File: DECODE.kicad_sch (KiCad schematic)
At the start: 16 parts

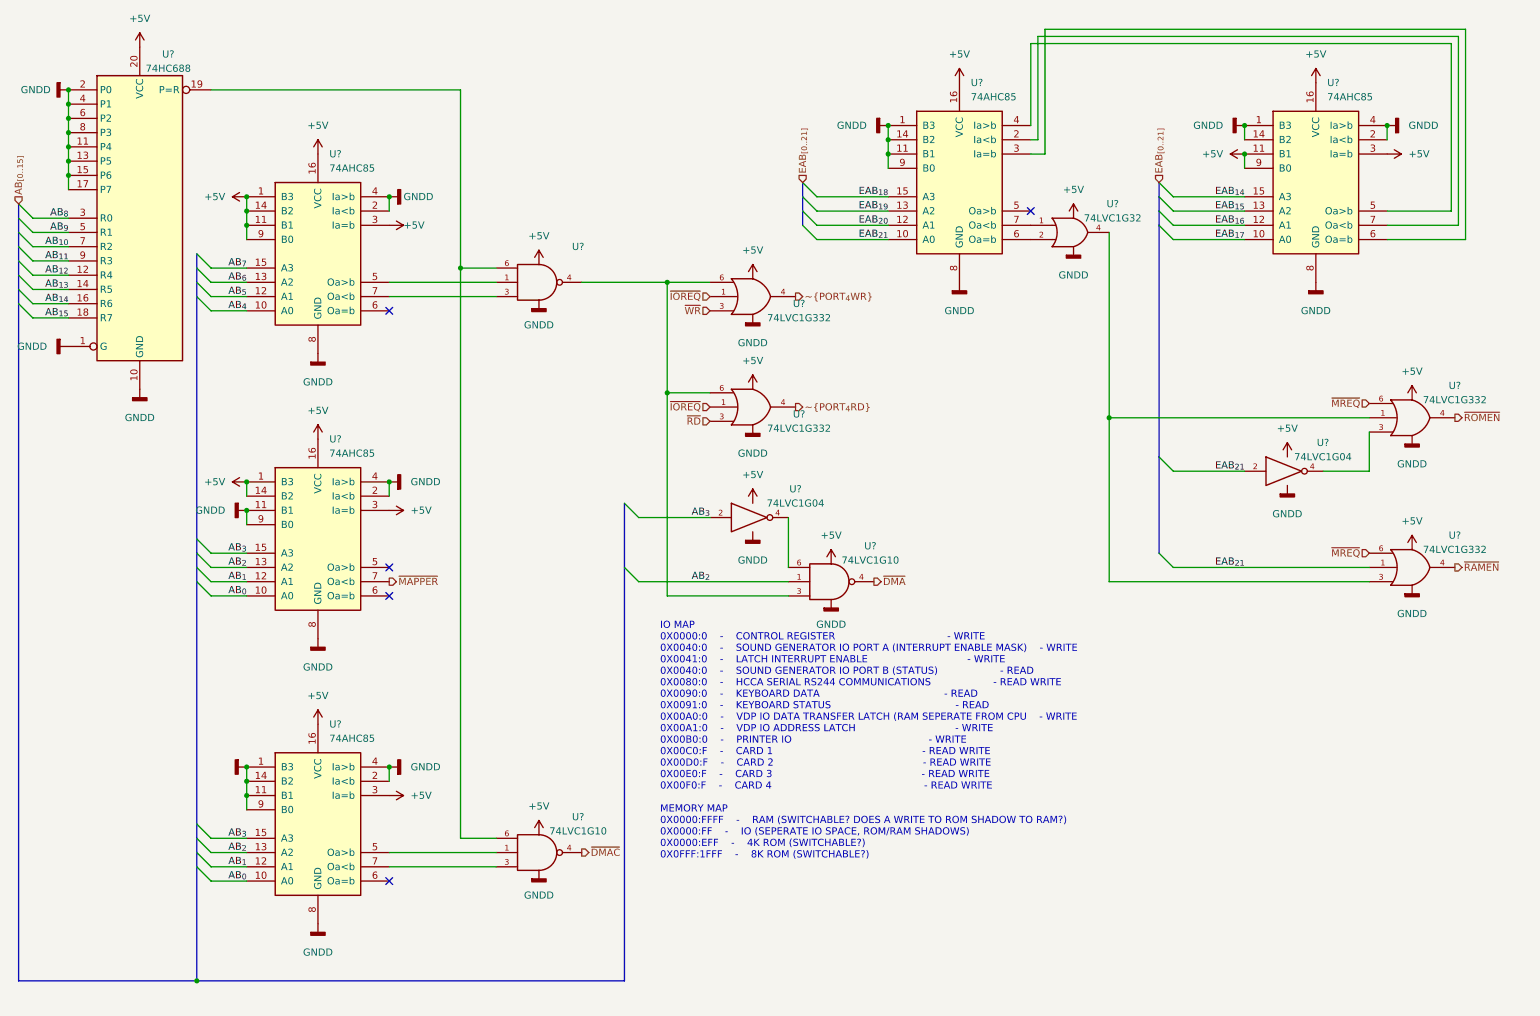
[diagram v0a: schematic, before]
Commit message: added decoupling capacitors, perhaps too many? idk better more than less!
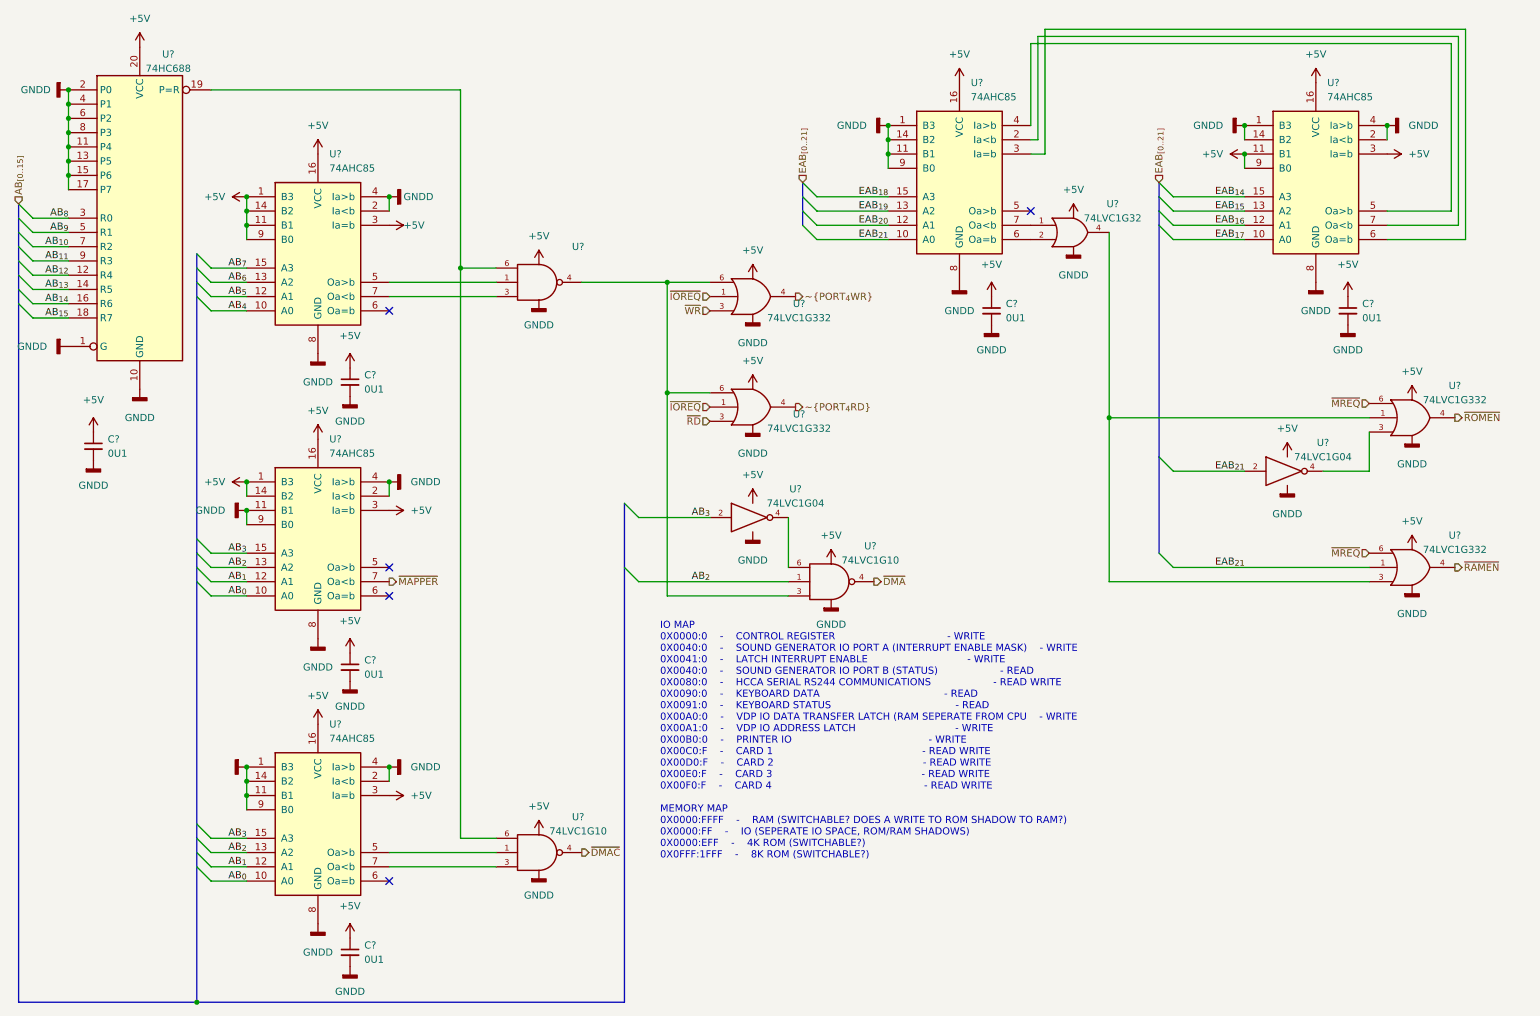
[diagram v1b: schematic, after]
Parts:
- added C? (x6): 0U1, symbol Device:C_Small
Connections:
- net +5V: now also C?.1, C?.1, C?.1, C?.1, C?.1, C?.1
- net GND: now also C?.2, C?.2, C?.2, C?.2, C?.2, C?.2

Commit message: some clean up and simplification, as well as some renaming
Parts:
- removed U?: ~, symbol 74xGxx:74LVC1G10
- added U63: (no value), symbol 74xGxx:74LVC1G10
- gave numbers to parts that had none: 21
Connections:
- net +5V: now also U63.5 (VCC)
- net GND: now also U63.2 (GND)
- net at U60.5 (Oa>b): now also U63.1
- net at U60.7 (Oa<b): now also U63.3
- net at U65.6, U66.6, U68.3: now also U63.4
- net at U59.19 (P=R), U64.6: now also U63.6
- net AB_{0} renamed AB0
- net AB_{10} renamed AB10
- net AB_{11} renamed AB11
- net AB_{12} renamed AB12
- net AB_{13} renamed AB13
- net AB_{14} renamed AB14
- net AB_{15} renamed AB15
- net AB_{1} renamed AB1
- net AB_{2} renamed AB2
- net AB_{3} renamed AB3
- net AB_{4} renamed AB4
- net AB_{5} renamed AB5
- net AB_{6} renamed AB6
- net AB_{7} renamed AB7
- net AB_{8} renamed AB8
- net AB_{9} renamed AB9
- net EAB_{14} renamed EAB14
- net EAB_{15} renamed EAB15
- net EAB_{16} renamed EAB16
- net EAB_{17} renamed EAB17
- net EAB_{18} renamed EAB18
- net EAB_{19} renamed EAB19
- net EAB_{20} renamed EAB20
- net EAB_{21} renamed EAB21

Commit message: begin integration of logic into atf1508
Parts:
- C33, C34, C35, C36, C37, C38: footprint (none) -> Capacitor_SMD:C_0603_1608Metric
- U59: footprint (none) -> Package_SO:TSSOP-20_4.4x6.5mm_P0.65mm
- U60, U61, U62, U69, U72: footprint (none) -> Package_SO:TSSOP-16_4.4x5mm_P0.65mm
- U63: value (none) -> 74LVC1G10; footprint (none) -> Package_TO_SOT_SMD:SOT-363_SC-70-6
- U64, U65, U66, U68, U73, U74: footprint (none) -> Package_TO_SOT_SMD:SOT-363_SC-70-6
- U67, U70, U71: footprint (none) -> Package_TO_SOT_SMD:SOT-353_SC-70-5
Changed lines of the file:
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@@
       (effects (font (size 1.27 1.27)) (justify left))
     )
-    (property "Footprint" "" (id 2) (at 247.65 48.26 0)
+    (property "Footprint" "Package_SO:TSSOP-16_4.4x5mm_P0.65mm" (id 2) (at 247.65 48.26 0)
       (effects (font (size 1.27 1.27)) hide)
     )
@@
       (effects (font (size 1.27 1.27)) (justify left))
     )
-    (property "Footprint" "" (id 2) (at 189.865 71.12 0)
+    (property "Footprint" "Capacitor_SMD:C_0603_1608Metric" (id 2) (at 189.865 71.12 0)
       (effects (font (size 1.27 1.27)) hide)
     )
@@
       (effects (font (size 1.27 1.27)) (justify left))
     )
-    (property "Footprint" "" (id 2) (at 69.85 60.96 0)
+    (property "Footprint" "Package_SO:TSSOP-16_4.4x5mm_P0.65mm" (id 2) (at 69.85 60.96 0)
       (effects (font (size 1.27 1.27)) hide)
     )
@@
     (property "Reference" "U66" (id 0) (at 155.575 89.535 0))
     (property "Value" "74LVC1G332" (id 1) (at 155.575 92.075 0))
-    (property "Footprint" "" (id 2) (at 147.32 88.265 0)
+    (property "Footprint" "Package_TO_SOT_SMD:SOT-363_SC-70-6" (id 2) (at 147.32 88.265 0)
       (effects (font (size 1.27 1.27)) hide)
     )
@@
     (property "Reference" "U59" (id 0) (at 43.18 25.4 0))
     (property "Value" "74HC688" (id 1) (at 43.18 27.94 0))
-    (property "Footprint" "" (id 2) (at 38.1 54.61 0)
+    (property "Footprint" "Package_SO:TSSOP-20_4.4x6.5mm_P0.65mm" (id 2) (at 38.1 54.61 0)
       (effects (font (size 1.27 1.27)) hide)
     )
@@
     (property "Reference" "U68" (id 0) (at 168.275 113.03 0))
     (property "Value" "74LVC1G10" (id 1) (at 168.275 115.57 0))
-    (property "Footprint" "" (id 2) (at 161.29 119.38 0)
+    (property "Footprint" "Package_TO_SOT_SMD:SOT-363_SC-70-6" (id 2) (at 161.29 119.38 0)
       (effects (font (size 1.27 1.27)) hide)
     )
@@
       (effects (font (size 1.27 1.27)) (justify left))
     )
-    (property "Footprint" "" (id 2) (at 69.85 111.76 0)
+    (property "Footprint" "Package_SO:TSSOP-16_4.4x5mm_P0.65mm" (id 2) (at 69.85 111.76 0)
       (effects (font (size 1.27 1.27)) hide)
     )
@@
       (effects (font (size 1.27 1.27)) (justify left))
     )
-    (property "Footprint" "" (id 2) (at 184.15 48.26 0)
+    (property "Footprint" "Package_SO:TSSOP-16_4.4x5mm_P0.65mm" (id 2) (at 184.15 48.26 0)
       (effects (font (size 1.27 1.27)) hide)
     )
@@
     (property "Reference" "U71" (id 0) (at 248.92 94.615 0))
     (property "Value" "74LVC1G04" (id 1) (at 248.92 97.155 0))
-    (property "Footprint" "" (id 2) (at 242.57 99.695 0)
+    (property "Footprint" "Package_TO_SOT_SMD:SOT-353_SC-70-5" (id 2) (at 242.57 99.695 0)
       (effects (font (size 1.27 1.27)) hide)
     )
@@
       (effects (font (size 1.27 1.27)) (justify left))
     )
-    (property "Footprint" "" (id 2) (at 75.565 185.42 0)
+    (property "Footprint" "Capacitor_SMD:C_0603_1608Metric" (id 2) (at 75.565 185.42 0)
       (effects (font (size 1.27 1.27)) hide)
     )
@@
       (effects (font (size 1.27 1.27)) (justify left))
     )
-    (property "Footprint" "" (id 2) (at 75.565 83.82 0)
+    (property "Footprint" "Capacitor_SMD:C_0603_1608Metric" (id 2) (at 75.565 83.82 0)
       (effects (font (size 1.27 1.27)) hide)
     )
@@
     (property "Reference" "U70" (id 0) (at 211.455 52.07 0))
     (property "Value" "74LVC1G32" (id 1) (at 211.455 54.61 0))
-    (property "Footprint" "" (id 2) (at 204.47 57.15 0)
+    (property "Footprint" "Package_TO_SOT_SMD:SOT-353_SC-70-5" (id 2) (at 204.47 57.15 0)
       (effects (font (size 1.27 1.27)) hide)
     )
@@
       (effects (font (size 1.27 1.27)) (justify left))
     )
-    (property "Footprint" "" (id 2) (at 29.845 95.25 0)
+    (property "Footprint" "Capacitor_SMD:C_0603_1608Metric" (id 2) (at 29.845 95.25 0)
       (effects (font (size 1.27 1.27)) hide)
     )
@@
       (effects (font (size 1.27 1.27)) (justify left))
     )
-    (property "Footprint" "" (id 2) (at 75.565 134.62 0)
+    (property "Footprint" "Capacitor_SMD:C_0603_1608Metric" (id 2) (at 75.565 134.62 0)
       (effects (font (size 1.27 1.27)) hide)
     )
@@
     (in_bom yes) (on_board yes)
     (property "Reference" "U63" (id 0) (at 116.205 67.945 0))
-    (property "Value" "" (id 1) (at 116.205 70.485 0))
-    (property "Footprint" "" (id 2) (at 109.22 66.04 0)
+    (property "Value" "74LVC1G10" (id 1) (at 116.205 70.485 0))
+    (property "Footprint" "Package_TO_SOT_SMD:SOT-363_SC-70-6" (id 2) (at 109.22 66.04 0)
       (effects (font (size 1.27 1.27)) hide)
     )
@@
     (property "Reference" "U67" (id 0) (at 154.94 102.87 0))
     (property "Value" "74LVC1G04" (id 1) (at 154.94 105.41 0))
-    (property "Footprint" "" (id 2) (at 147.32 107.95 0)
+    (property "Footprint" "Package_TO_SOT_SMD:SOT-353_SC-70-5" (id 2) (at 147.32 107.95 0)
       (effects (font (size 1.27 1.27)) hide)
     )
@@
     (property "Reference" "U73" (id 0) (at 272.415 84.455 0))
     (property "Value" "74LVC1G332" (id 1) (at 272.415 86.995 0))
-    (property "Footprint" "" (id 2) (at 264.795 90.17 0)
+    (property "Footprint" "Package_TO_SOT_SMD:SOT-363_SC-70-6" (id 2) (at 264.795 90.17 0)
       (effects (font (size 1.27 1.27)) hide)
     )
@@
       (effects (font (size 1.27 1.27)) (justify left))
     )
-    (property "Footprint" "" (id 2) (at 253.365 71.12 0)
+    (property "Footprint" "Capacitor_SMD:C_0603_1608Metric" (id 2) (at 253.365 71.12 0)
       (effects (font (size 1.27 1.27)) hide)
     )
@@
       (effects (font (size 1.27 1.27)) (justify left))
     )
-    (property "Footprint" "" (id 2) (at 69.85 162.56 0)
+    (property "Footprint" "Package_SO:TSSOP-16_4.4x5mm_P0.65mm" (id 2) (at 69.85 162.56 0)
       (effects (font (size 1.27 1.27)) hide)
     )
@@
     (property "Reference" "U64" (id 0) (at 116.205 161.29 0))
     (property "Value" "74LVC1G10" (id 1) (at 116.205 163.83 0))
-    (property "Footprint" "" (id 2) (at 109.22 167.64 0)
+    (property "Footprint" "Package_TO_SOT_SMD:SOT-363_SC-70-6" (id 2) (at 109.22 167.64 0)
       (effects (font (size 1.27 1.27)) hide)
     )
@@
     (property "Reference" "U74" (id 0) (at 272.415 111.125 0))
     (property "Value" "74LVC1G332" (id 1) (at 272.415 113.665 0))
-    (property "Footprint" "" (id 2) (at 264.795 116.84 0)
+    (property "Footprint" "Package_TO_SOT_SMD:SOT-363_SC-70-6" (id 2) (at 264.795 116.84 0)
       (effects (font (size 1.27 1.27)) hide)
     )
@@
     (property "Reference" "U65" (id 0) (at 155.575 69.85 0))
     (property "Value" "74LVC1G332" (id 1) (at 155.575 72.39 0))
-    (property "Footprint" "" (id 2) (at 147.32 68.58 0)
-      (effects (font (size 1.27 1.27)) hide)
-    )
+    (property "Footprint" "Package_TO_SOT_SMD:SOT-363_SC-70-6" (id 2) (at 147.32 68.58 0)
+      (effects (font (size 1.27 1.27)) hide)
+    )
